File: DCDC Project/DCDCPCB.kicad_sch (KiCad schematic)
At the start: 31 parts, among them J1 IPL1, J2 IPL1, J3 IPL1, J4 MPT-04, K1 RELAY_SPDT

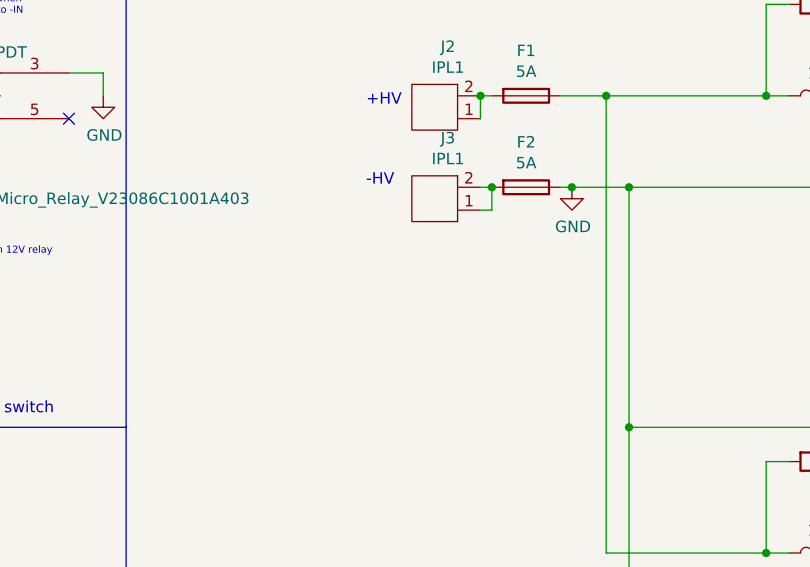
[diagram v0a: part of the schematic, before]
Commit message: Updating schematic for voltage
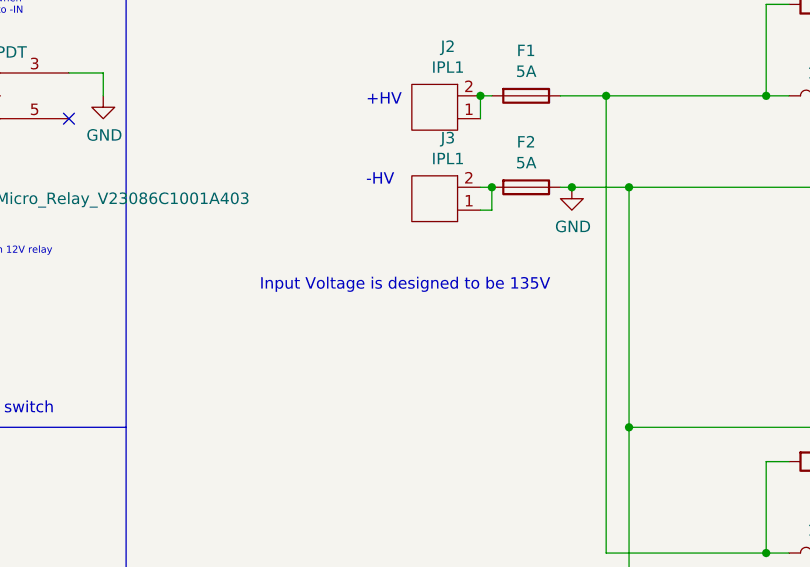
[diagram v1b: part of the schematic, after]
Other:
- note added: "Input Voltage is designed to be 135V"
